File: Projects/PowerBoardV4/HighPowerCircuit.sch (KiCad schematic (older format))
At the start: 21 parts, among them J1 Cell Voltage Sense, J10 5V_INT_PWR_BLK, J12 12V_INT_PWR_BLK, J2 BATT_PWR, J3 12V POWER SUPPLY, J4 5V POWER SUPPLY, J5 BACK_EXT_24V, J7 MC_STACK_1, J8 MC_STACK_2, J9 24V_INT_PWR_BLK, Q1 IRF3205, Q2 IRF3205, Q3 BSS84

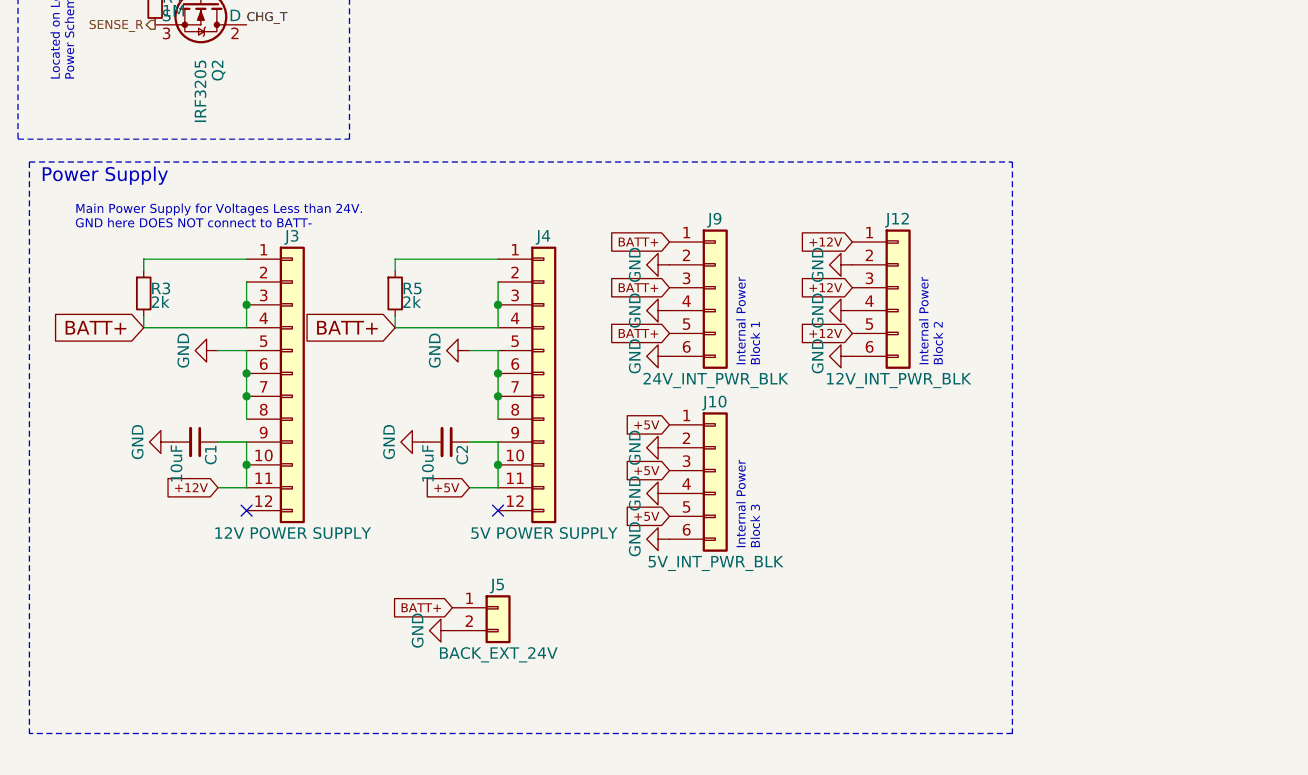
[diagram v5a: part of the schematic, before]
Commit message: Fixing unconnected connections, added 5V connections
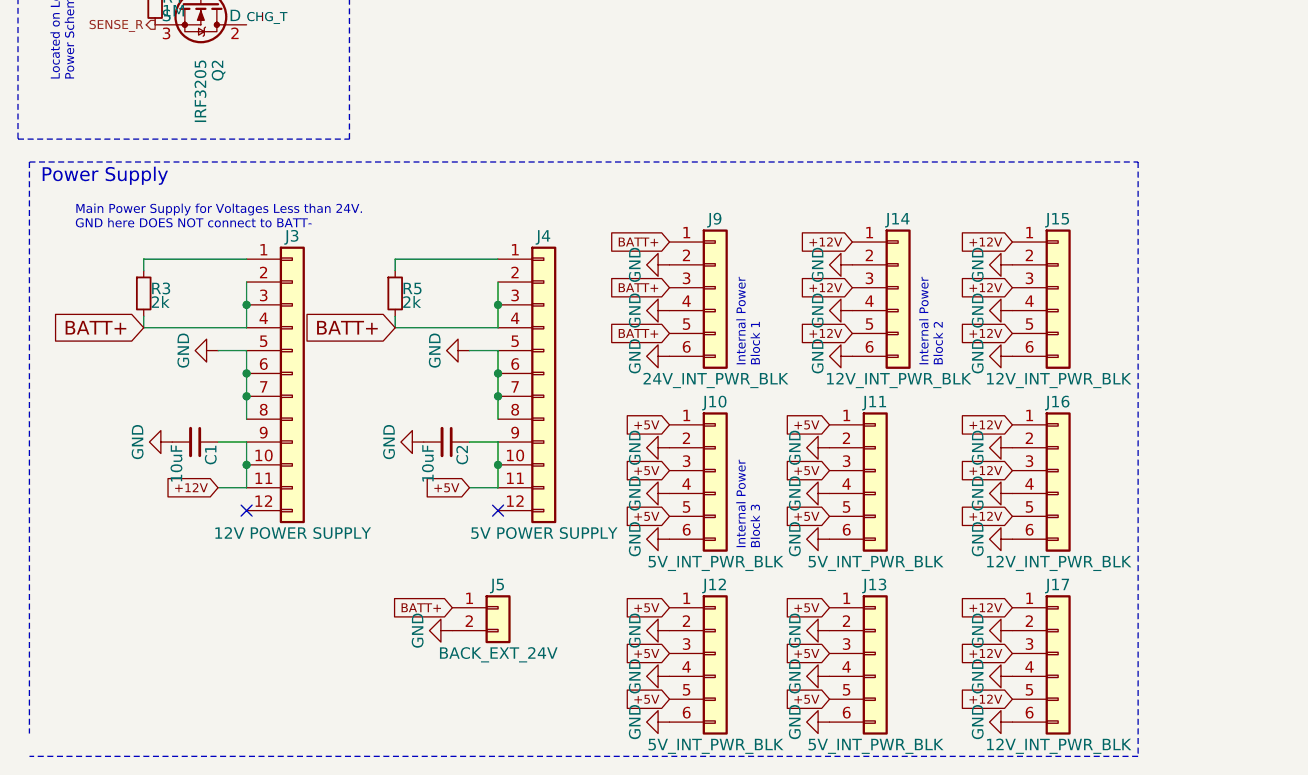
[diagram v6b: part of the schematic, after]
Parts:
- added J11, J12, J13: 5V_INT_PWR_BLK, Terminal_Blocks:TerminalBlock_Pheonix_PT-3.5mm_6pol, symbol Conn_01x06
- added J15, J16, J17: 12V_INT_PWR_BLK, USST-footprints:TerminalBlock_Pheonix_PT-5mm_6pol, symbol Conn_01x06
- renumbered J12 to J14
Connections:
- net +12V: now also J15.1 (Pin_1), J15.3 (Pin_3), J15.5 (Pin_5), J16.1 (Pin_1), J16.3 (Pin_3), J16.5 (Pin_5), J17.1 (Pin_1), J17.3 (Pin_3), J17.5 (Pin_5)
- net +5V: now also J11.1 (Pin_1), J11.3 (Pin_3), J11.5 (Pin_5), J12.1 (Pin_1), J12.3 (Pin_3), J12.5 (Pin_5), J13.1 (Pin_1), J13.3 (Pin_3), J13.5 (Pin_5)
- net GND: now also J11.2 (Pin_2), J11.4 (Pin_4), J11.6 (Pin_6), J12.2 (Pin_2), J12.4 (Pin_4), J12.6 (Pin_6), J13.2 (Pin_2), J13.4 (Pin_4), J13.6 (Pin_6), J15.2 (Pin_2), J15.4 (Pin_4), J15.6 (Pin_6), J16.2 (Pin_2), J16.4 (Pin_4), J16.6 (Pin_6), J17.2 (Pin_2), J17.4 (Pin_4), J17.6 (Pin_6)

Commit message: Changes complete and ready for review
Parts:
- removed J11, J12, J13: 5V_INT_PWR_BLK, Terminal_Blocks:TerminalBlock_Pheonix_PT-3.5mm_6pol, symbol Conn_01x06
- removed J15, J16, J17: 12V_INT_PWR_BLK, USST-footprints:TerminalBlock_Pheonix_PT-5mm_6pol, symbol Conn_01x06
- added J11, J12, J6: 5V-Extra, USST-footprints:Molex_39531_1002, symbol Conn_01x02
- added J13, J15, J16: 12V-Extra, USST-footprints:Molex_39531_1002, symbol Conn_01x02
- J14: footprint USST-footprints:TerminalBlock_Pheonix_PT-5mm_6pol -> Terminal_Blocks:TerminalBlock_Pheonix_PT-3.5mm_6pol
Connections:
- net +12V: now also J13.1 (Pin_1), J15.1 (Pin_1), J16.1 (Pin_1)
- net +5V: now also J11.1 (Pin_1), J12.1 (Pin_1), J6.1 (Pin_1)
- net GND: now also J11.2 (Pin_2), J12.2 (Pin_2), J13.2 (Pin_2), J15.2 (Pin_2), J16.2 (Pin_2), J6.2 (Pin_2)

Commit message: Did some more stuff
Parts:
- removed J3: 12V POWER SUPPLY, USST-footprints:R-6212P_14-34VDC-12VDC_Converter, symbol Conn_01x12
- removed R3: 2k, Resistors_SMD:R_0603, symbol R_Small
- added C3: 6.8uF, symbol C_Small
- added C4: 6.8 nF, symbol C_Small
- added J3: 12V 60W PWR Supp, symbol Conn_01x06
- added L1: 4.8 uH, symbol L_Small
- C1: value 10uF -> 100uF; footprint Capacitors_ThroughHole:C_Radial_D5_L11_P2.5 -> (none)
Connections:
- net +12V: now also J3.5 (Pin_5); no longer C1.1
- net BATT+: now also C1.2, L1.1
- net GND: now also C1.1, C3.1, C4.2, J3.2 (Pin_2); no longer C1.2
- new net: C3.2, J3.1 (Pin_1), L1.2
- new net: C4.1, J3.6 (Pin_6)
- no-connect marks 2 -> 1
